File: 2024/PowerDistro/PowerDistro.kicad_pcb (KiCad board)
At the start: 4 copper layers, 280 x 230 mm, 89 parts, among them J1 10159560-A00221RLF, J18 Conn_01x02_Pin, J19 4 Pin JST-GH, J2 10159560-A00221RLF, J20 4 Pin JST-GH, J21 4 Pin JST-GH, J22 4 Pin JST-GH, J3 10159560-A00221RLF, J4 10159560-A00221RLF, J5 10159560-A00221RLF, J6 10159560-A00221RLF, J7 10159560-A00221RLF, J8 10159560-A00221RLF, U1 PCA9685

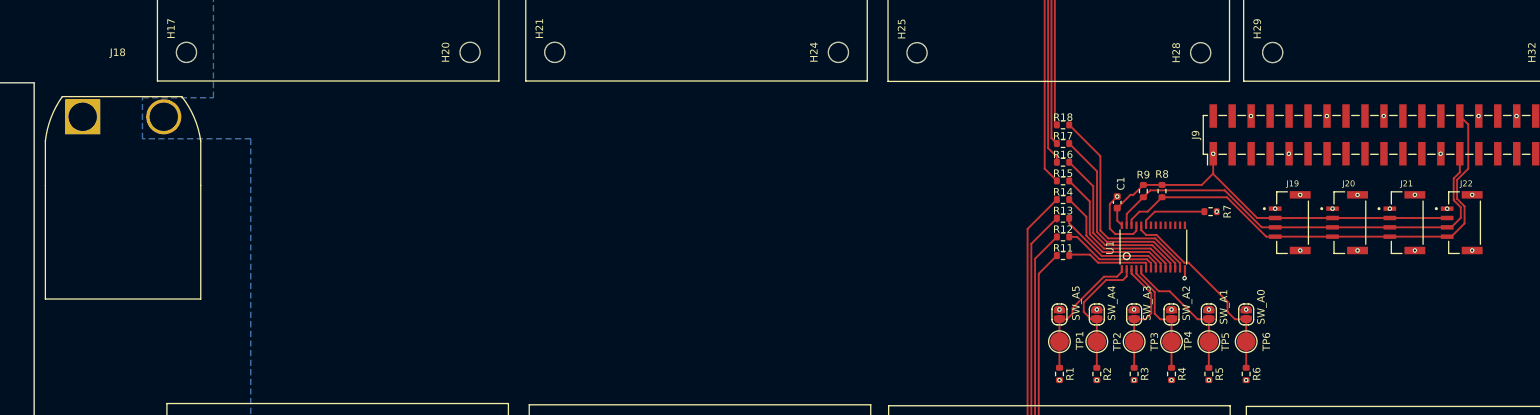
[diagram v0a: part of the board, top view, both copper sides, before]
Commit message: Fixed 3d models
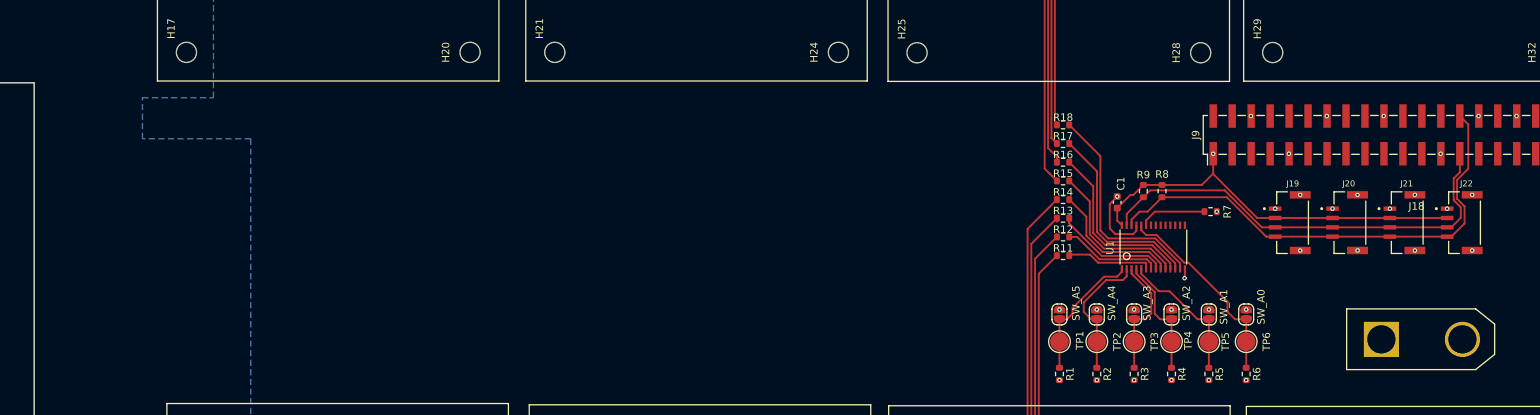
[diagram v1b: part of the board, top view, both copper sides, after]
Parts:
- moved J18 175.1 mm to (359.4, 146.3)

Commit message: Changed Everything
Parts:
- removed H1, H10, H11, H12, H13, H14, H15, H16, H17, H18, H19, H2, H20, H21, H22, H23, H24, H25, H26, H27, H28, H29, H3, H30, H31, H32, H4, H5, H6, H7, H8, H9: MountingHole, MountingHole:MountingHole_2.7mm_M2.5_ISO7380
- removed H33, H34, H35, H36: MountingHole, MountingHole:MountingHole_4.3mm_M4_ISO7380
- removed J17: ~, PowerDistroFootprints:MR30PB
- removed TP1, TP2, TP3, TP4, TP5, TP6: TestPoint, TestPoint:TestPoint_Pad_D2.5mm
- added R10: 220, Resistor_SMD:R_0603_1608Metric, F.Cu at (310.7, 158.0)
- added R19: 220, Resistor_SMD:R_0603_1608Metric, F.Cu at (313.2, 158.0)
- added R20: 220, Resistor_SMD:R_0603_1608Metric, F.Cu at (315.7, 158.0)
- added R21: 220, Resistor_SMD:R_0603_1608Metric, F.Cu at (318.2, 158.0)
- added R22: 220, Resistor_SMD:R_0603_1608Metric, F.Cu at (320.7, 158.0)
- added R23: 220, Resistor_SMD:R_0603_1608Metric, F.Cu at (323.2, 158.0)
- added R24: 220, Resistor_SMD:R_0603_1608Metric, F.Cu at (325.8, 158.0)
- added R25: 220, Resistor_SMD:R_0603_1608Metric, F.Cu at (328.3, 158.0)
- added U2: ~, PowerDistroFootprints:BlueRoboticsESC, F.Cu at (227.8, 177.3)
- added U3: ~, PowerDistroFootprints:BlueRoboticsESC, F.Cu at (264.2, 177.3)
- added U4: ~, PowerDistroFootprints:BlueRoboticsESC, F.Cu at (191.2, 177.3)
- added U5: ~, PowerDistroFootprints:BlueRoboticsESC, F.Cu at (191.2, 104.0)
- added U6: ~, PowerDistroFootprints:BlueRoboticsESC, F.Cu at (227.8, 104.0)
- added U7: ~, PowerDistroFootprints:BlueRoboticsESC, F.Cu at (264.2, 104.0)
- J1, J2, J3, J4, J5, J6: value 10159560-A00221RLF -> Screw_Terminal_01x03; footprint PowerDistroFootprints:AMPHENOL_10159560-A00221RLF -> PowerDistroFootprints:691311500103
- J10, J11, J12, J13, J14, J15, J16: value ~ -> Screw_Terminal_01x02; footprint PowerDistroFootprints:MR30PB -> PowerDistroFootprints:691311500102
- J19, J20, J21, J22: footprint PowerDistroFootprints:JST_BM04B-GHS-TBT_LF__SN__N_ -> Connector_JST:JST_XH_B4B-XH-A_1x04_P2.50mm_Vertical
- J7, J8: value 10159560-A00221RLF -> Conn_01x02_Pin; footprint PowerDistroFootprints:AMPHENOL_10159560-A00221RLF -> Connector_PinHeader_2.54mm:PinHeader_1x02_P2.54mm_Vertical
- J9: value ~ -> Conn_01x05_Pin; footprint Connector_PinHeader_2.54mm:PinHeader_2x20_P2.54mm_Vertical_SMD -> Connector_PinHeader_2.54mm:PinHeader_1x05_P2.54mm_Vertical
- moved J10 219.9 mm to (170.2, 128.0), turned to -90 degrees
- moved J16 205.7 mm to (170.2, 185.5), turned to -90 degrees
- moved J11 165.9 mm to (170.2, 153.0), turned to -90 degrees
- moved J15 165.5 mm to (170.2, 172.0), turned to -90 degrees
- moved J4 144.4 mm to (191.2, 75.0), turned to 0 degrees
- moved J12 134.5 mm to (170.2, 140.5), turned to -90 degrees
- moved J13 133.6 mm to (170.2, 109.5), turned to -90 degrees
- moved J1 132.9 mm to (227.8, 206.3)
- moved J8 126.3 mm to (300.8, 162.0)
- moved J7 113.5 mm to (295.8, 162.0)
- moved J9 90.8 mm to (298.2, 189.0), turned to 180 degrees
- moved J21 82.9 mm to (312.5, 199.5), turned to 0 degrees
- moved J18 75.2 mm to (284.2, 142.0), turned to -90 degrees
- moved J14 74.5 mm to (170.2, 95.5), turned to -90 degrees
- moved J3 73.7 mm to (191.2, 206.3)
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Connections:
- J1 pad 1: PVDD -> Net-(J1-Pin_1)
- J1 pad 2: PVDD -> Net-(J1-Pin_2)
- J1 pad 3: GND -> Net-(J1-Pin_3)
- J10 pad 1: 1MOT_A -> PVDD
- J10 pad 2: 1MOT_B -> GND
- J11 pad 1: 2MOT_A -> PVDD
- J11 pad 2: 2MOT_B -> GND
- J12 pad 1: 3MOT_A -> PVDD
- J12 pad 2: 3MOT_B -> GND
- J13 pad 1: 4MOT_A -> PVDD
- J13 pad 2: 4MOT_B -> GND
- J14 pad 1: 5MOT_A -> PVDD
- J14 pad 2: 5MOT_B -> GND
- J15 pad 1: 6MOT_A -> PVDD
- J15 pad 2: 6MOT_B -> GND
- J16 pad 1: 7MOT_A -> PVDD
- J16 pad 2: 7MOT_B -> GND
- J2 pad 1: PVDD -> Net-(J2-Pin_1)
- J2 pad 2: PVDD -> Net-(J2-Pin_2)
- J2 pad 3: GND -> Net-(J2-Pin_3)
- J3 pad 1: PVDD -> Net-(J3-Pin_1)
- J3 pad 2: PVDD -> Net-(J3-Pin_2)
- J3 pad 3: GND -> Net-(J3-Pin_3)
- J4 pad 1: PVDD -> Net-(J4-Pin_1)
- J4 pad 2: PVDD -> Net-(J4-Pin_2)
- J4 pad 3: GND -> Net-(J4-Pin_3)
- J5 pad 1: PVDD -> Net-(J5-Pin_1)
- J5 pad 2: PVDD -> Net-(J5-Pin_2)
- J5 pad 3: GND -> Net-(J5-Pin_3)
- J6 pad 1: PVDD -> Net-(J6-Pin_1)
- J6 pad 2: PVDD -> Net-(J6-Pin_2)
- J6 pad 3: GND -> Net-(J6-Pin_3)
- J7 pad 1: PVDD -> PWM7
- J7 pad 2: PVDD -> GND
- J8 pad 1: PVDD -> PWM8
- J8 pad 2: PVDD -> GND
- J9 pad 2: 5.0_VDC -> I2C5_DAT
- J9 pad 3: I2C5_DAT -> I2C5_CLK
- J9 pad 4: 5.0_VDC -> MCLK05
- J9 pad 5: I2C5_CLK -> GND
- R11 pad 2: COM1 -> PWM1
- R12 pad 2: COM2 -> PWM2
- R13 pad 2: COM3 -> PWM3
- R14 pad 2: COM4 -> PWM4
- R15 pad 2: COM5 -> PWM5
- R16 pad 2: COM6 -> PWM6
- R17 pad 2: COM7 -> PWM7
- R18 pad 2: COM8 -> PWM8
- U1 pad 15: unconnected-(U1-PWM8-Pad15) -> Net-(U1-PWM8)
- U1 pad 16: unconnected-(U1-PWM9-Pad16) -> Net-(U1-PWM9)
- U1 pad 17: unconnected-(U1-PWM10-Pad17) -> Net-(U1-PWM10)
- U1 pad 18: unconnected-(U1-PWM11-Pad18) -> Net-(U1-PWM11)
- U1 pad 19: unconnected-(U1-PWM12-Pad19) -> Net-(U1-PWM12)
- U1 pad 20: unconnected-(U1-PWM13-Pad20) -> Net-(U1-PWM13)
- U1 pad 21: unconnected-(U1-PWM14-Pad21) -> Net-(U1-PWM14)
- U1 pad 22: unconnected-(U1-PWM15-Pad22) -> Net-(U1-PWM15)
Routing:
- net PWM1: track 0.00 -> 221.1 mm
- net PWM6: track 0.00 -> 214.4 mm, vias 0 -> 2
- net COM4: track 188.7 -> 0.00 mm
- net PWM2: track 0.00 -> 184.3 mm
- net PWM5: track 0.00 -> 176.8 mm, vias 0 -> 2
- net COM5: track 155.2 -> 0.00 mm
- net COM3: track 138.2 -> 0.00 mm
- net COM8: track 119.4 -> 0.00 mm
- net COM1: track 119.3 -> 0.00 mm
- net COM6: track 103.8 -> 0.00 mm
- net COM2: track 88.2 -> 0.00 mm
- net GND: track 12.7 -> 87.9 mm, vias 564 -> 172
- net COM7: track 74.7 -> 0.00 mm
- net I2C2_CLK: track 65.7 -> 0.00 mm
- net I2C2_DAT: track 60.0 -> 0.00 mm
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- added copper zone on B.Cu, net GND
- added copper zone on F.Cu, net Net-(J1-Pin_1)
- added copper zone on F.Cu, net Net-(J1-Pin_2)
- added copper zone on F.Cu, net Net-(J1-Pin_3)
- added copper zone on F.Cu, net Net-(J2-Pin_1)
- added copper zone on F.Cu, net Net-(J2-Pin_2)
- added copper zone on F.Cu, net Net-(J2-Pin_3)
- added copper zone on F.Cu, net Net-(J3-Pin_1)
- added copper zone on F.Cu, net Net-(J3-Pin_2)
- added copper zone on F.Cu, net Net-(J3-Pin_3)
- added copper zone on F.Cu, net Net-(J4-Pin_1)
- added copper zone on F.Cu, net Net-(J4-Pin_2)
- added copper zone on F.Cu, net Net-(J4-Pin_3)
- added copper zone on F.Cu, net Net-(J5-Pin_1)
- added copper zone on F.Cu, net Net-(J5-Pin_2)
- added copper zone on F.Cu, net Net-(J5-Pin_3)
- added copper zone on F.Cu, net Net-(J6-Pin_1)
- added copper zone on F.Cu, net Net-(J6-Pin_2)
- added copper zone on F.Cu, net Net-(J6-Pin_3)
- removed copper zone on F.Cu, net 1MOT_A
- removed copper zone on F.Cu, net 1MOT_B
- removed copper zone on F.Cu, net 1MOT_C
- removed copper zone on F.Cu, net 2MOT_A
- removed copper zone on F.Cu, net 2MOT_B
- removed copper zone on F.Cu, net 2MOT_C
- removed copper zone on F.Cu, net 3MOT_A
- removed copper zone on F.Cu, net 3MOT_B
- removed copper zone on F.Cu, net 3MOT_C
- removed copper zone on F.Cu, net 4MOT_A
- removed copper zone on F.Cu, net 4MOT_B
- removed copper zone on F.Cu, net 4MOT_C
- removed copper zone on F.Cu, net 5MOT_A
- removed copper zone on F.Cu, net 5MOT_B
- removed copper zone on F.Cu, net 5MOT_C
- removed copper zone on F.Cu, net 6MOT_A
- removed copper zone on F.Cu, net 6MOT_B
- removed copper zone on F.Cu, net 6MOT_C
- removed copper zone on F.Cu, net 7MOT_A
- removed copper zone on F.Cu, net 7MOT_B
- removed copper zone on F.Cu, net 7MOT_C
- removed copper zone on F.Cu, net 8MOT_A
- removed copper zone on F.Cu, net 8MOT_B
- removed copper zone on F.Cu, net 8MOT_C
- removed copper zone on B.Cu, net PVDD

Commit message: Release
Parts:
- removed the J13 at (170.2, 109.5)
- added H1: MountingHole, MountingHole:MountingHole_5.3mm_M5, F.Cu at (80.5, 30.5)
- added H2: MountingHole, MountingHole:MountingHole_5.3mm_M5, F.Cu at (338.5, 30.5)
- added H3: MountingHole, MountingHole:MountingHole_5.3mm_M5, F.Cu at (80.5, 238.5)
- added H4: MountingHole, MountingHole:MountingHole_5.3mm_M5, F.Cu at (339.5, 238.5)
- added J15: Screw_Terminal_01x02, PowerDistroFootprints:691321100002, F.Cu at (146.0, 132.2)
- added J17: Screw_Terminal_01x02, PowerDistroFootprints:691321100002, F.Cu at (162.5, 160.0)
- added J23: Screw_Terminal_01x02, PowerDistroFootprints:691321100002, F.Cu at (162.5, 146.2)
- added J24: Screw_Terminal_01x02, PowerDistroFootprints:691321100002, F.Cu at (162.5, 132.2)
- added J25: Screw_Terminal_01x02, PowerDistroFootprints:691321100002, F.Cu at (162.5, 117.8)
- added Q1: IRLML6344, Package_TO_SOT_SMD:SOT-23, F.Cu at (153.2, 161.7)
- added Q2: IRLML6344, Package_TO_SOT_SMD:SOT-23, F.Cu at (153.2, 147.9)
- added Q3: IRLML6344, Package_TO_SOT_SMD:SOT-23, F.Cu at (153.2, 133.9)
- added Q4: IRLML6344, Package_TO_SOT_SMD:SOT-23, F.Cu at (153.2, 119.4)
- added Q5: IRLML6344, Package_TO_SOT_SMD:SOT-23, F.Cu at (169.8, 161.7)
- added Q6: IRLML6344, Package_TO_SOT_SMD:SOT-23, F.Cu at (169.8, 147.9)
- added Q7: IRLML6344, Package_TO_SOT_SMD:SOT-23, F.Cu at (169.8, 133.9)
- added Q8: IRLML6344, Package_TO_SOT_SMD:SOT-23, F.Cu at (169.8, 119.4)
- added R26: 10k, Resistor_SMD:R_0603_1608Metric, F.Cu at (153.2, 166.0)
- added R27: 10k, Resistor_SMD:R_0603_1608Metric, F.Cu at (145.7, 166.0)
- added R28: 10k, Resistor_SMD:R_0603_1608Metric, F.Cu at (145.7, 152.2)
- added R29: 10k, Resistor_SMD:R_0603_1608Metric, F.Cu at (153.2, 152.2)
- added R30: 10k, Resistor_SMD:R_0603_1608Metric, F.Cu at (145.7, 138.2)
- added R31: 10k, Resistor_SMD:R_0603_1608Metric, F.Cu at (153.2, 138.2)
- added R32: 10k, Resistor_SMD:R_0603_1608Metric, F.Cu at (145.7, 123.8)
- added R33: 10k, Resistor_SMD:R_0603_1608Metric, F.Cu at (153.2, 123.8)
- added R34: 10k, Resistor_SMD:R_0603_1608Metric, F.Cu at (162.2, 166.0)
- added R35: 10k, Resistor_SMD:R_0603_1608Metric, F.Cu at (162.2, 152.2)
- added R36: 10k, Resistor_SMD:R_0603_1608Metric, F.Cu at (162.2, 138.2)
- added R37: 10k, Resistor_SMD:R_0603_1608Metric, F.Cu at (162.2, 123.8)
- added R38: 10k, Resistor_SMD:R_0603_1608Metric, F.Cu at (169.7, 166.0)
- added R39: 10k, Resistor_SMD:R_0603_1608Metric, F.Cu at (169.7, 152.2)
- added R40: 10k, Resistor_SMD:R_0603_1608Metric, F.Cu at (169.7, 138.2)
- added R41: 10k, Resistor_SMD:R_0603_1608Metric, F.Cu at (169.7, 123.8)
- C1: footprint Capacitor_SMD:C_0603_1608Metric -> Capacitor_SMD:C_1206_3216Metric
- J10, J11, J12, J14, J16: footprint PowerDistroFootprints:691311500102 -> PowerDistroFootprints:691321100002
- J13: renamed from J15; footprint PowerDistroFootprints:691311500102 -> PowerDistroFootprints:691321100002
- J18: value Conn_01x02_Pin -> XT90
- moved J16 72.0 mm to (146.0, 117.8), turned to 0 degrees
- moved J14 56.2 mm to (146.0, 146.2), turned to 0 degrees
- moved J9 52.6 mm to (344.5, 164.0), turned to -90 degrees
- moved J19 46.4 mm to (343.0, 203.0), turned to 180 degrees
- moved J21 41.1 mm to (343.0, 172.0), turned to 180 degrees
- moved J22 34.0 mm to (343.0, 193.0), turned to 180 degrees
- moved J20 31.3 mm to (343.0, 182.5), turned to 180 degrees
- moved J13 27.1 mm to (146.0, 160.0), turned to 0 degrees
- moved R7 18.7 mm to (322.3, 140.0)
- moved C1 17.2 mm to (323.0, 135.5), turned to 0 degrees
- moved R9 16.3 mm to (332.0, 136.2)
- moved R24 16.0 mm to (309.9, 155.5), turned to -90 degrees
- moved R10 14.5 mm to (325.0, 155.5), turned to -90 degrees
- moved R19 14.5 mm to (327.5, 155.5), turned to -90 degrees
- moved R8 12.3 mm to (332.0, 139.5), turned to 90 degrees
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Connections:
- J13 pad 2: GND -> Net-(J13-Pin_2)
- J14 pad 2: GND -> Net-(J14-Pin_2)
- J16 pad 2: GND -> Net-(J16-Pin_2)
- J18 pad 1: PVDD -> GND
- J18 pad 2: GND -> PVDD
- J19 pad 3: I2C2_DAT -> I2C_DAT
- J19 pad 4: I2C2_CLK -> I2C_CLK
- J20 pad 3: I2C2_DAT -> I2C_DAT
- J20 pad 4: I2C2_CLK -> I2C_CLK
- J21 pad 3: I2C2_DAT -> I2C_DAT
- J21 pad 4: I2C2_CLK -> I2C_CLK
- J22 pad 3: I2C2_DAT -> I2C_DAT
- J22 pad 4: I2C2_CLK -> I2C_CLK
- J9 pad 2: I2C5_DAT -> I2C_DAT
- J9 pad 3: I2C5_CLK -> I2C_CLK
- R8 pad 2: I2C2_CLK -> I2C_CLK
- R9 pad 2: I2C2_DAT -> I2C_DAT
- U1 pad 26: I2C2_CLK -> I2C_CLK
- U1 pad 27: I2C2_DAT -> I2C_DAT
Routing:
- net PWM12: track 0.00 -> 294.4 mm
- net PWM11: track 0.00 -> 284.1 mm
- net PWM9: track 0.00 -> 274.4 mm
- net PWM16: track 0.00 -> 271.3 mm
- net PWM10: track 0.00 -> 264.7 mm
- net PWM15: track 0.00 -> 260.4 mm
- net PWM14: track 0.00 -> 250.6 mm
- net GND: track 87.9 -> 337.7 mm, vias 172 -> 284
- net PWM13: track 0.00 -> 241.1 mm
- net 3.3_VDC: track 49.4 -> 140.7 mm, vias 6 -> 8
- net I2C_DAT: track 0.00 -> 87.7 mm
- net I2C_CLK: track 0.00 -> 83.7 mm
- net PVDD: track 0.00 -> 50.0 mm
- net Net-(U1-PWM15): track 0.00 -> 19.4 mm
- net Net-(U1-PWM14): track 0.00 -> 17.4 mm
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- removed copper zone on In2.Cu, net 3.3_VDC
- removed copper zone on In1.Cu, net GND
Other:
- copper layers 4 -> 2
- board text added: "+"
- board text added: "-"
- board text added: "3.3V"
- board text added: "GND"
- board text added: "I2C_CLK"
- board text added: "I2C_DAT"
- board text added: "MCLK05"
- board text added: "RoboCats Main Board Designed Poorly by Peter Buckley at 3am"

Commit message: fixed a tiny trace issue
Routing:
- net 3.3_VDC: track 140.7 -> 140.2 mm
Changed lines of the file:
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@@
 		(tags "connector JST XH vertical")
 		(property "Reference" "J21"
-			(at 3.75 -3.55 360)
+			(at 3.75 -3.55 0)
 			(layer "F.SilkS")
 			(effects
@@
 		)
 		(property "Value" "4 Pin JST-GH"
-			(at 3.75 4.6 360)
+			(at 3.75 4.6 0)
 			(layer "F.Fab")
 			(effects
@@
 		)
 		(fp_text user "${REFERENCE}"
-			(at 3.75 2.7 360)
+			(at 3.75 2.7 0)
 			(layer "F.Fab")
 			(effects
@@
 		(tags "resistor")
 		(property "Reference" "R36"
-			(at 0 1.5 360)
+			(at 0 1.5 0)
 			(layer "F.SilkS")
 			(effects
@@
 		)
 		(property "Value" "10k"
-			(at 0 1.43 360)
+			(at 0 1.43 0)
 			(layer "F.Fab")
 			(effects
@@
 		)
 		(fp_text user "${REFERENCE}"
-			(at 0 0 360)
+			(at 0 0 0)
 			(layer "F.Fab")
 			(effects
@@
 		)
 		(property "Value" "Conn_01x05_Pin"
-			(at -8.34 62.055 360)
+			(at -8.34 62.055 0)
 			(layer "F.Fab")
 			(effects
@@
 		)
 		(fp_text user "${REFERENCE}"
-			(at 0 5.08 360)
+			(at 0 5.08 0)
 			(layer "F.Fab")
 			(effects
@@
 		(tags "resistor")
 		(property "Reference" "R29"
-			(at 0 1.5 360)
+			(at 0 1.5 0)
 			(layer "F.SilkS")
 			(effects
@@
 		)
 		(property "Value" "10k"
-			(at 0 1.43 360)
+			(at 0 1.43 0)
 			(layer "F.Fab")
 			(effects
@@
 		)
 		(fp_text user "${REFERENCE}"
-			(at 0 0 360)
+			(at 0 0 0)
 			(layer "F.Fab")
 			(effects
@@
 		(tags "resistor")
 		(property "Reference" "R32"
-			(at 0 1.5 360)
+			(at 0 1.5 0)
 			(layer "F.SilkS")
 			(effects
@@
 		)
 		(property "Value" "10k"
-			(at 0 1.43 360)
+			(at 0 1.43 0)
 			(layer "F.Fab")
 			(effects
@@
 		)
 		(fp_text user "${REFERENCE}"
-			(at 0 0 360)
+			(at 0 0 0)
 			(layer "F.Fab")
 			(effects
@@
 		(tags "resistor")
 		(property "Reference" "R37"
-			(at 0 1.5 360)
+			(at 0 1.5 0)
 			(layer "F.SilkS")
 			(effects
@@
 		)
 		(property "Value" "10k"
-			(at 0 1.43 360)
+			(at 0 1.43 0)
 			(layer "F.Fab")
 			(effects
@@
 		)
 		(fp_text user "${REFERENCE}"
-			(at 0 0 360)
+			(at 0 0 0)
 			(layer "F.Fab")
 			(effects
@@
 		(tags "resistor")
 		(property "Reference" "R38"
-			(at 0 1.5 360)
+			(at 0 1.5 0)
 			(layer "F.SilkS")
 			(effects
@@
 		)
 		(property "Value" "10k"
-			(at 0 1.43 360)
+			(at 0 1.43 0)
 			(layer "F.Fab")
 			(effects
@@
 		)
 		(fp_text user "${REFERENCE}"
-			(at 0 0 360)
+			(at 0 0 0)
 			(layer "F.Fab")
 			(effects
@@
 		(tags "resistor")
 		(property "Reference" "R39"
-			(at 0 1.5 360)
+			(at 0 1.5 0)
 			(layer "F.SilkS")
 			(effects
@@
 		)
 		(property "Value" "10k"
-			(at 0 1.43 360)
+			(at 0 1.43 0)
 			(layer "F.Fab")
 			(effects
@@
 		)
 		(fp_text user "${REFERENCE}"
-			(at 0 0 360)
+			(at 0 0 0)
 			(layer "F.Fab")
 			(effects
@@
 		(tags "resistor")
 		(property "Reference" "R8"
-			(at -2.25 0 360)
+			(at -2.25 0 0)
 			(layer "F.SilkS")
 			(effects
@@
 		)
 		(property "Value" "10k"
-			(at -3.5 -0.25 360)
+			(at -3.5 -0.25 0)
 			(layer "F.Fab")
 			(effects
@@
 		(tags "resistor")
 		(property "Reference" "R26"
-			(at 0 1.5 360)
+			(at 0 1.5 0)
 			(layer "F.SilkS")
 			(effects
@@
 		)
 		(property "Value" "10k"
-			(at 0 1.43 360)
+			(at 0 1.43 0)
 			(layer "F.Fab")
 			(effects
@@
 		)
 		(fp_text user "${REFERENCE}"
-			(at 0 0 360)
+			(at 0 0 0)
 			(layer "F.Fab")
 			(effects
@@
 		(tags "resistor")
 		(property "Reference" "R28"
-			(at 0 1.5 360)
+			(at 0 1.5 0)
 			(layer "F.SilkS")
 			(effects
@@
 		)
 		(property "Value" "10k"
-			(at 0 1.43 360)
+			(at 0 1.43 0)
 			(layer "F.Fab")
 			(effects
@@
 		)
 		(fp_text user "${REFERENCE}"
-			(at 0 0 360)
+			(at 0 0 0)
 			(layer "F.Fab")
 			(effects
@@
 		(tags "resistor")
 		(property "Reference" "R33"
-			(at 0 1.5 360)
+			(at 0 1.5 0)
 			(layer "F.SilkS")
 			(effects
@@
 		)
 		(property "Value" "10k"
-			(at 0 1.43 360)
+			(at 0 1.43 0)
 			(layer "F.Fab")
 			(effects
@@
 		)
 		(fp_text user "${REFERENCE}"
-			(at 0 0 360)
+			(at 0 0 0)
 			(layer "F.Fab")
 			(effects
@@
 		(tags "resistor")
 		(property "Reference" "R41"
-			(at 0 1.5 360)
+			(at 0 1.5 0)
 			(layer "F.SilkS")
 			(effects
@@
 		)
 		(property "Value" "10k"
-			(at 0 1.43 360)
+			(at 0 1.43 0)
 			(layer "F.Fab")
 			(effects
@@
 		)
 		(fp_text user "${REFERENCE}"
-			(at 0 0 360)
+			(at 0 0 0)
 			(layer "F.Fab")
 			(effects
@@
 		(tags "resistor")
 		(property "Reference" "R40"
-			(at 0 1.5 360)
+			(at 0 1.5 0)
 			(layer "F.SilkS")
 			(effects
@@
 		)
 		(property "Value" "10k"
-			(at 0 1.43 360)
+			(at 0 1.43 0)
 			(layer "F.Fab")
 			(effects
@@
 		)
 		(fp_text user "${REFERENCE}"
-			(at 0 0 360)
+			(at 0 0 0)
 			(layer "F.Fab")
 			(effects
@@
 		(tags "connector JST XH vertical")
 		(property "Reference" "J20"
-			(at 3.75 -3.55 360)
+			(at 3.75 -3.55 0)
 			(layer "F.SilkS")
 			(effects
@@
 		)
 		(property "Value" "4 Pin JST-GH"
-			(at 3.75 4.6 360)
+			(at 3.75 4.6 0)
 			(layer "F.Fab")
 			(effects
@@
 		)
 		(fp_text user "${REFERENCE}"
-			(at 3.75 2.7 360)
+			(at 3.75 2.7 0)
 			(layer "F.Fab")
 			(effects
@@
 		(tags "connector JST XH vertical")
 		(property "Reference" "J22"
-			(at 3.75 -3.55 360)
+			(at 3.75 -3.55 0)
 			(layer "F.SilkS")
 			(effects
@@
 		)
 		(property "Value" "4 Pin JST-GH"
-			(at 3.75 4.6 360)
+			(at 3.75 4.6 0)
 			(layer "F.Fab")
 			(effects
@@
 		)
 		(fp_text user "${REFERENCE}"
-			(at 3.75 2.7 360)
+			(at 3.75 2.7 0)
 			(layer "F.Fab")
 			(effects
@@
 		(tags "resistor")
 		(property "Reference" "R30"
-			(at 0 1.5 360)
+			(at 0 1.5 0)
 			(layer "F.SilkS")
 			(effects
@@
 		)
 		(property "Value" "10k"
-			(at 0 1.43 360)
+			(at 0 1.43 0)
 			(layer "F.Fab")
 			(effects
@@
 		)
 		(fp_text user "${REFERENCE}"
-			(at 0 0 360)
+			(at 0 0 0)
 			(layer "F.Fab")
 			(effects
@@
 		(tags "resistor")
 		(property "Reference" "R31"
-			(at 0 1.5 360)
+			(at 0 1.5 0)
 			(layer "F.SilkS")
 			(effects
@@
 		)
 		(property "Value" "10k"
-			(at 0 1.43 360)
+			(at 0 1.43 0)
 			(layer "F.Fab")
 			(effects
@@
 		)
 		(fp_text user "${REFERENCE}"
-			(at 0 0 360)
+			(at 0 0 0)
 			(layer "F.Fab")
 			(effects
@@
 		(tags "resistor")
 		(property "Reference" "R35"
-			(at 0 1.5 360)
+			(at 0 1.5 0)
 			(layer "F.SilkS")
 			(effects
@@
 		)
 		(property "Value" "10k"
-			(at 0 1.43 360)
+			(at 0 1.43 0)
 			(layer "F.Fab")
 			(effects
@@
 		)
 		(fp_text user "${REFERENCE}"
-			(at 0 0 360)
+			(at 0 0 0)
 			(layer "F.Fab")
 			(effects
@@
 		(tags "resistor")
 		(property "Reference" "R27"
-			(at 0 1.5 360)
+			(at 0 1.5 0)
 			(layer "F.SilkS")
 			(effects
@@
 		)
 		(property "Value" "10k"
-			(at 0 1.43 360)
+			(at 0 1.43 0)
 			(layer "F.Fab")
 			(effects
@@
 		)
 		(fp_text user "${REFERENCE}"
-			(at 0 0 360)
+			(at 0 0 0)
 			(layer "F.Fab")
 			(effects
@@
 		(tags "resistor")
 		(property "Reference" "R34"
-			(at 0 1.5 360)
+			(at 0 1.5 0)
 			(layer "F.SilkS")
 			(effects
@@
 		)
 		(property "Value" "10k"
-			(at 0 1.43 360)
+			(at 0 1.43 0)
 			(layer "F.Fab")
 			(effects
@@
 		)
 		(fp_text user "${REFERENCE}"
-			(at 0 0 360)
+			(at 0 0 0)
 			(layer "F.Fab")
 			(effects
@@
 		(tags "connector JST XH vertical")
 		(property "Reference" "J19"
-			(at 3.75 4.525 360)
+			(at 3.75 4.525 0)
 			(layer "F.SilkS")
 			(effects
@@
 		)
 		(property "Value" "4 Pin JST-GH"
-			(at 3.75 4.6 360)
+			(at 3.75 4.6 0)
 			(layer "F.Fab")
 			(effects
@@
 		)
 		(fp_text user "${REFERENCE}"
-			(at 3.75 2.7 360)
+			(at 3.75 2.7 0)
 			(layer "F.Fab")
 			(effects
@@
 		(layer "F.Cu")
 		(net 1)
-	)
-	(segment
-		(start 330 132)
-		(end 330.5 132)
-		(width 0.254)
-		(layer "F.Cu")
-		(net 1)

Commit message: Got rid of peter's "did poorly statement"
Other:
- board text removed: "RoboCats Main Board Designed Poorly by Peter Buckley at 3am"
